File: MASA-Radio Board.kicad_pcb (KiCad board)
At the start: 4 copper layers, 75.8 x 76.2 mm, 71 parts, among them IC1 FAN4010IL6X_F113, IC2 FAN4010IL6X_F113, J1 Conn_01x02, J2 Conn_01x02_Male, J3 Conn_01x02_Male, J4 Conn_01x03_Male, J5 Conn_01x06, J6 SC_19-20, J7 Conn_01x06, J8 Conn_01x02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

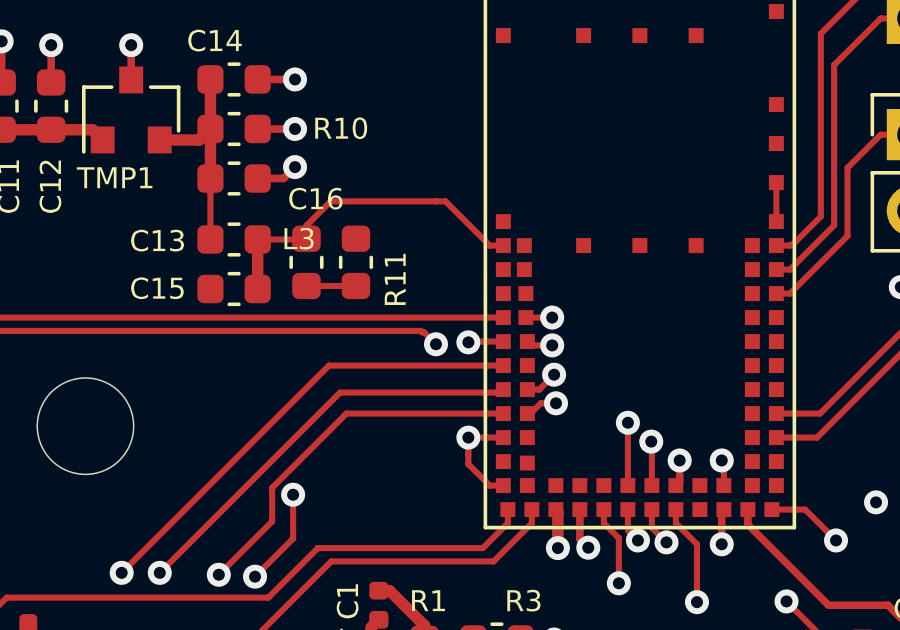
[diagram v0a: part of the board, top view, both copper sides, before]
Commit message: fixed tsense
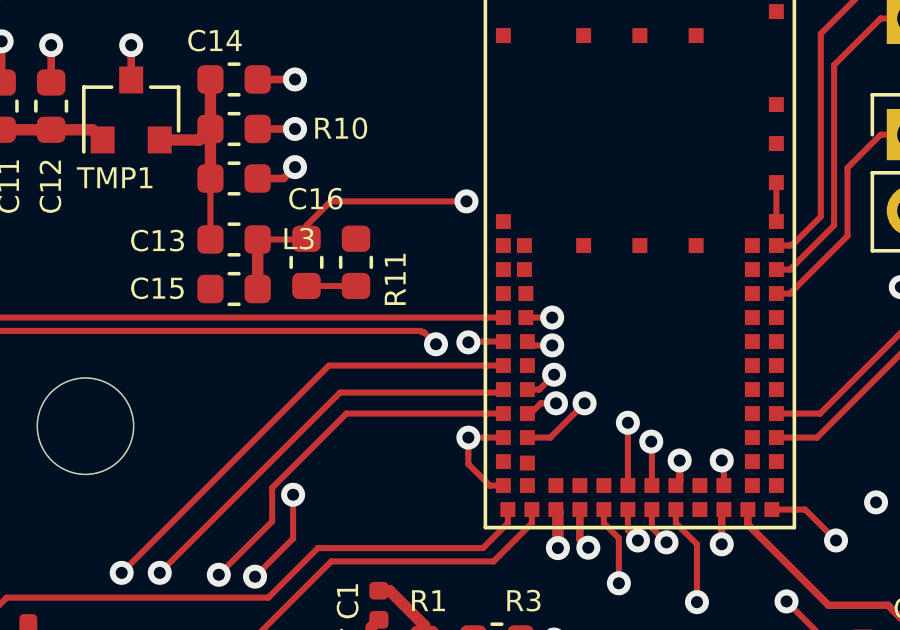
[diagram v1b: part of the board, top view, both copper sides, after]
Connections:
- U2 pad 48: Net-(U2-Pad48) -> TSENSE
- U2 pad 63: TSENSE -> Net-(U2-Pad63)
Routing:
- net TSENSE: track 11.2 -> 20.1 mm, vias 0 -> 2
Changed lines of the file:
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@@
     (thickness 1.6)
     (drawings 18)
-    (tracks 702)
+    (tracks 707)
     (zones 0)
     (modules 71)
@@
   (net 38 "Net-(U2-Pad60)")
   (net 39 "Net-(U2-Pad54)")
-  (net 40 "Net-(U2-Pad48)")
-  (net 41 "Net-(U2-Pad46)")
+  (net 40 "Net-(U2-Pad46)")
+  (net 41 "Net-(U2-Pad63)")
   (net 42 "Net-(U2-Pad61)")
   (net 43 "Net-(U2-Pad59)")
@@
     (add_net "Net-(U2-Pad45)")
     (add_net "Net-(U2-Pad46)")
-    (add_net "Net-(U2-Pad48)")
     (add_net "Net-(U2-Pad54)")
     (add_net "Net-(U2-Pad59)")
@@
     (add_net "Net-(U2-Pad61)")
     (add_net "Net-(U2-Pad62)")
+    (add_net "Net-(U2-Pad63)")
     (add_net "Net-(U2-Pad64)")
     (add_net "Net-(U2-Pad7)")
@@
       (net 26 TX2RTS))
     (pad 48 smd rect (at -3.75 8.15) (size 0.5 0.5) (layers F.Cu F.Paste F.Mask)
-      (net 40 "Net-(U2-Pad48)"))
+      (net 72 TSENSE))
     (pad 46 smd rect (at -3.75 9) (size 0.5 0.5) (layers F.Cu F.Paste F.Mask)
-      (net 41 "Net-(U2-Pad46)"))
+      (net 40 "Net-(U2-Pad46)"))
     (pad 65 smd rect (at -4.55 0.95) (size 0.5 0.5) (layers F.Cu F.Paste F.Mask)
       (net 1 GND))
     (pad 63 smd rect (at -4.55 1.75) (size 0.5 0.5) (layers F.Cu F.Paste F.Mask)
-      (net 72 TSENSE))
+      (net 41 "Net-(U2-Pad63)"))
     (pad 61 smd rect (at -4.55 2.55) (size 0.5 0.5) (layers F.Cu F.Paste F.Mask)
       (net 42 "Net-(U2-Pad61)"))
@@
   (segment (start 152.7 109.107114) (end 152.700889 109.106225) (width 0.2032) (layer F.Cu) (net 14))
   (segment (start 152.7 111.2) (end 152.7 109.107114) (width 0.2032) (layer F.Cu) (net 14))
-  (segment (start 152.700889 109.106225) (end 150.418275 109.106225) (width 0.2032) (layer In2.Cu) (net 14))
-  (segment (start 147.193 112.3315) (end 128.9685 112.3315) (width 0.2032) (layer In2.Cu) (net 14))
-  (segment (start 150.418275 109.106225) (end 147.193 112.3315) (width 0.2032) (layer In2.Cu) (net 14))
-  (segment (start 128.9685 112.3315) (end 126.746 114.554) (width 0.2032) (layer In2.Cu) (net 14))
+  (segment (start 150.418275 109.106225) (end 152.700889 109.106225) (width 0.2032) (layer In2.Cu) (net 14))
+  (segment (start 126.746 114.554) (end 128.7145 112.5855) (width 0.2032) (layer In2.Cu) (net 14))
+  (segment (start 146.939 112.5855) (end 150.418275 109.106225) (width 0.2032) (layer In2.Cu) (net 14))
+  (segment (start 128.7145 112.5855) (end 146.939 112.5855) (width 0.2032) (layer In2.Cu) (net 14))
   (segment (start 153.5 111.2) (end 153.5 111.168) (width 0.254) (layer F.Cu) (net 15))
   (via (at 127.889 114.681) (size 0.8) (drill 0.4) (layers F.Cu B.Cu) (net 15))
@@
   (segment (start 153.5 111.2) (end 153.5 109.755325) (width 0.2032) (layer F.Cu) (net 15))
   (segment (start 153.5 109.755325) (end 153.4795 109.734825) (width 0.2032) (layer F.Cu) (net 15))
-  (segment (start 153.4795 109.734825) (end 150.424675 109.734825) (width 0.2032) (layer In2.Cu) (net 15))
-  (segment (start 150.424675 109.734825) (end 147.3835 112.776) (width 0.2032) (layer In2.Cu) (net 15))
-  (segment (start 147.3835 112.776) (end 129.794 112.776) (width 0.2032) (layer In2.Cu) (net 15))
-  (segment (start 129.794 112.776) (end 127.889 114.681) (width 0.2032) (layer In2.Cu) (net 15))
+  (segment (start 150.424675 109.734825) (end 153.4795 109.734825) (width 0.2032) (layer In2.Cu) (net 15))
+  (segment (start 147.1295 113.03) (end 150.424675 109.734825) (width 0.2032) (layer In2.Cu) (net 15))
+  (segment (start 127.889 114.681) (end 129.54 113.03) (width 0.2032) (layer In2.Cu) (net 15))
+  (segment (start 129.54 113.03) (end 147.1295 113.03) (width 0.2032) (layer In2.Cu) (net 15))
   (segment (start 154.3 111.2) (end 154.253 111.2) (width 0.254) (layer F.Cu) (net 16))
   (via (at 154.426471 110.363425) (size 0.8) (drill 0.4) (layers F.Cu B.Cu) (net 16))
@@
   (via (at 129.032 114.681) (size 0.8) (drill 0.4) (layers F.Cu B.Cu) (net 16))
   (segment (start 128.905 114.808) (end 129.032 114.681) (width 0.254) (layer F.Cu) (net 16))
-  (segment (start 130.3655 113.3475) (end 147.701 113.3475) (width 0.2032) (layer In2.Cu) (net 16))
-  (segment (start 150.685075 110.363425) (end 154.426471 110.363425) (width 0.2032) (layer In2.Cu) (net 16))
-  (segment (start 147.701 113.3475) (end 150.685075 110.363425) (width 0.2032) (layer In2.Cu) (net 16))
-  (segment (start 129.032 114.681) (end 130.3655 113.3475) (width 0.2032) (layer In2.Cu) (net 16))
+  (segment (start 129.032 114.681) (end 130.232101 113.480899) (width 0.2032) (layer In2.Cu) (net 16))
+  (segment (start 150.685075 110.363425) (end 147.574 113.4745) (width 0.2032) (layer In2.Cu) (net 16))
+  (segment (start 130.232101 113.480899) (end 147.32 113.4745) (width 0.2032) (layer In2.Cu) (net 16))
+  (segment (start 147.574 113.4745) (end 147.32 113.4745) (width 0.2032) (layer In2.Cu) (net 16))
+  (segment (start 154.426471 110.363425) (end 150.685075 110.363425) (width 0.2032) (layer In2.Cu) (net 16))
+  (segment (start 147.32 113.4745) (end 147.504101 113.480899) (width 0.2032) (layer In2.Cu) (net 16))
   (via (at 155.0035 115.085801) (size 0.8) (drill 0.4) (layers F.Cu B.Cu) (net 17))
   (segment (start 155.0035 114.520116) (end 155.0035 115.085801) (width 0.2032) (layer F.Cu) (net 17))
@@
   (segment (start 141.9605 102.997) (end 141.986 102.9715) (width 0.2032) (layer F.Cu) (net 72))
   (segment (start 140.3605 102.997) (end 141.9605 102.997) (width 0.2032) (layer F.Cu) (net 72))
-  (segment (start 141.986 102.534) (end 142.793 101.727) (width 0.2032) (layer F.Cu) (net 72))
-  (segment (start 141.986 102.9715) (end 141.986 102.534) (width 0.2032) (layer F.Cu) (net 72))
-  (segment (start 146.6238 101.727) (end 146.304 101.727) (width 0.2032) (layer F.Cu) (net 72))
-  (segment (start 148.0968 103.2) (end 146.6238 101.727) (width 0.2032) (layer F.Cu) (net 72))
-  (segment (start 148.55 103.2) (end 148.0968 103.2) (width 0.2032) (layer F.Cu) (net 72))
-  (segment (start 142.793 101.727) (end 146.304 101.727) (width 0.2032) (layer F.Cu) (net 72))
+  (via (at 147.32 101.727) (size 0.8) (drill 0.4) (layers F.Cu B.Cu) (net 72))
+  (segment (start 141.986 102.534) (end 141.986 102.9715) (width 0.2032) (layer F.Cu) (net 72))
+  (segment (start 147.32 101.727) (end 142.793 101.727) (width 0.2032) (layer F.Cu) (net 72))
+  (segment (start 142.793 101.727) (end 141.986 102.534) (width 0.2032) (layer F.Cu) (net 72))
+  (via (at 151.257 108.458) (size 0.8) (drill 0.4) (layers F.Cu B.Cu) (net 72))
+  (segment (start 151.257 108.458) (end 150.115 109.6) (width 0.2032) (layer F.Cu) (net 72))
+  (segment (start 150.115 109.6) (end 149.35 109.6) (width 0.2032) (layer F.Cu) (net 72))
+  (segment (start 151.257 105.664) (end 147.32 101.727) (width 0.2032) (layer In2.Cu) (net 72))
+  (segment (start 151.257 108.458) (end 151.257 105.664) (width 0.2032) (layer In2.Cu) (net 72))
   (segment (start 174.609 130.0385) (end 175.768 128.8795) (width 0.2032) (layer F.Cu) (net 74))
   (segment (start 174.609 130.206) (end 174.609 130.0385) (width 0.2032) (layer F.Cu) (net 74))

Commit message: Added caps on 3.3V MCU
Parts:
- added C26: 100uF, Capacitor_SMD:C_0603_1608Metric, F.Cu at (165.0, 116.2)
- added C27: 1uF, Capacitor_SMD:C_0603_1608Metric, F.Cu at (169.0, 116.2)
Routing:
- net +3V3: track 25.6 -> 42.9 mm, vias 5 -> 6
- net GND: track 106.6 -> 109.2 mm, vias 59 -> 61
- net V_IN_5V0: track 113.1 -> 112.2 mm
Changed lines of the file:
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@@
     (thickness 1.6)
     (drawings 18)
-    (tracks 707)
+    (tracks 718)
     (zones 0)
-    (modules 71)
+    (modules 73)
     (nets 134)
   )
@@
     (add_net nAutoRun)
   )
+  (module Capacitor_SMD:C_0603_1608Metric (layer F.Cu)
+    (at 169.0465 116.205)
+    (descr "Capacitor SMD 0603 (1608 Metric), square (rectangular) end terminal, IPC_7351 nominal, (Body size source: http://www.tortai-tech.com/upload/download/2011102023233369053.pdf), generated with kicad-footprint-generator")
+    (tags capacitor)
+    (attr smd)
+    (fp_text reference C27 (at 0.7525 -1.4605) (layer F.SilkS)
+      (effects (font (size 1 1) (thickness 0.15)))
+    )
+    (fp_text value 1uF (at 0 1.43) (layer F.Fab)
+      (effects (font (size 1 1) (thickness 0.15)))
+    )
+    (fp_line (start -0.8 0.4) (end -0.8 -0.4) (layer F.Fab) (width 0.1))
+    (fp_line (start -0.8 -0.4) (end 0.8 -0.4) (layer F.Fab) (width 0.1))
+    (fp_line (start 0.8 -0.4) (end 0.8 0.4) (layer F.Fab) (width 0.1))
+    (fp_line (start 0.8 0.4) (end -0.8 0.4) (layer F.Fab) (width 0.1))
+    (fp_line (start -0.162779 -0.51) (end 0.162779 -0.51) (layer F.SilkS) (width 0.12))
+    (fp_line (start -0.162779 0.51) (end 0.162779 0.51) (layer F.SilkS) (width 0.12))
+    (fp_line (start -1.48 0.73) (end -1.48 -0.73) (layer F.CrtYd) (width 0.05))
+    (fp_line (start -1.48 -0.73) (end 1.48 -0.73) (layer F.CrtYd) (width 0.05))
+    (fp_line (start 1.48 -0.73) (end 1.48 0.73) (layer F.CrtYd) (width 0.05))
+    (fp_line (start 1.48 0.73) (end -1.48 0.73) (layer F.CrtYd) (width 0.05))
+    (fp_text user %R (at 0 0) (layer F.Fab)
+      (effects (font (size 0.4 0.4) (thickness 0.06)))
+    )
+    (pad 1 smd roundrect (at -0.7875 0) (size 0.875 0.95) (layers F.Cu F.Paste F.Mask) (roundrect_rratio 0.25)
+      (net 8 +3V3))
+    (pad 2 smd roundrect (at 0.7875 0) (size 0.875 0.95) (layers F.Cu F.Paste F.Mask) (roundrect_rratio 0.25)
+      (net 1 GND))
+    (model ${KISYS3DMOD}/Capacitor_SMD.3dshapes/C_0603_1608Metric.wrl
+      (at (xyz 0 0 0))
+      (scale (xyz 1 1 1))
+      (rotate (xyz 0 0 0))
+    )
+  )
+  (module Capacitor_SMD:C_0603_1608Metric (layer F.Cu)
+    (at 165.0365 116.205)
+    (descr "Capacitor SMD 0603 (1608 Metric), square (rectangular) end terminal, IPC_7351 nominal, (Body size source: http://www.tortai-tech.com/upload/download/2011102023233369053.pdf), generated with kicad-footprint-generator")
+    (tags capacitor)
+    (attr smd)
+    (fp_text reference C26 (at 0.889 -1.4605) (layer F.SilkS)
+      (effects (font (size 1 1) (thickness 0.15)))
+    )
+    (fp_text value 100uF (at 0 1.43) (layer F.Fab)
+      (effects (font (size 1 1) (thickness 0.15)))
+    )
+    (fp_line (start -0.8 0.4) (end -0.8 -0.4) (layer F.Fab) (width 0.1))
+    (fp_line (start -0.8 -0.4) (end 0.8 -0.4) (layer F.Fab) (width 0.1))
+    (fp_line (start 0.8 -0.4) (end 0.8 0.4) (layer F.Fab) (width 0.1))
+    (fp_line (start 0.8 0.4) (end -0.8 0.4) (layer F.Fab) (width 0.1))
+    (fp_line (start -0.162779 -0.51) (end 0.162779 -0.51) (layer F.SilkS) (width 0.12))
+    (fp_line (start -0.162779 0.51) (end 0.162779 0.51) (layer F.SilkS) (width 0.12))
+    (fp_line (start -1.48 0.73) (end -1.48 -0.73) (layer F.CrtYd) (width 0.05))
+    (fp_line (start -1.48 -0.73) (end 1.48 -0.73) (layer F.CrtYd) (width 0.05))
+    (fp_line (start 1.48 -0.73) (end 1.48 0.73) (layer F.CrtYd) (width 0.05))
+    (fp_line (start 1.48 0.73) (end -1.48 0.73) (layer F.CrtYd) (width 0.05))
+    (fp_text user %R (at 0 0) (layer F.Fab)
+      (effects (font (size 0.4 0.4) (thickness 0.06)))
+    )
+    (pad 1 smd roundrect (at -0.7875 0) (size 0.875 0.95) (layers F.Cu F.Paste F.Mask) (roundrect_rratio 0.25)
+      (net 8 +3V3))
+    (pad 2 smd roundrect (at 0.7875 0) (size 0.875 0.95) (layers F.Cu F.Paste F.Mask) (roundrect_rratio 0.25)
+      (net 1 GND))
+    (model ${KISYS3DMOD}/Capacitor_SMD.3dshapes/C_0603_1608Metric.wrl
+      (at (xyz 0 0 0))
+      (scale (xyz 1 1 1))
+      (rotate (xyz 0 0 0))
+    )
+  )
   (module Connector_PinHeader_2.54mm:PinHeader_1x06_P2.54mm_Vertical (layer F.Cu)
     (at 179.959 104.267 230)
@@
   (segment (start 149.35 108) (end 149.7465 108) (width 0.2032) (layer F.Cu) (net 1))
   (segment (start 149.7465 108) (end 150.241 107.5055) (width 0.2032) (layer F.Cu) (net 1))
+  (via (at 167.0685 116.205) (size 0.8) (drill 0.4) (layers F.Cu B.Cu) (net 1))
+  (segment (start 165.824 116.205) (end 167.0685 116.205) (width 0.2032) (layer F.Cu) (net 1))
+  (via (at 171.196 116.205) (size 0.8) (drill 0.4) (layers F.Cu B.Cu) (net 1))
+  (segment (start 169.834 116.205) (end 171.196 116.205) (width 0.2032) (layer F.Cu) (net 1))
   (segment (start 160.655 126.4742) (end 161.925 127.7442) (width 0.2032) (layer F.Cu) (net 2))
   (segment (start 160.655 126.3142) (end 160.655 126.4742) (width 0.2032) (layer F.Cu) (net 2))
@@
   (segment (start 130.683 128.524) (end 132.461 128.524) (width 0.381) (layer F.Cu) (net 8))
   (segment (start 129.747 129.46) (end 130.1115 129.0955) (width 0.381) (layer F.Cu) (net 8))
-  (segment (start 155.9 112) (end 155.9 112.085) (width 0.25) (layer F.Cu) (net 8))
-  (via (at 155.829 113.157) (size 0.8) (drill 0.4) (layers F.Cu B.Cu) (net 8))
-  (segment (start 155.9 112.085) (end 155.829 112.156) (width 0.25) (layer F.Cu) (net 8))
-  (segment (start 155.829 112.156) (end 155.829 113.157) (width 0.25) (layer F.Cu) (net 8))
   (via (at 150.241 116.332) (size 0.8) (drill 0.4) (layers F.Cu B.Cu) (net 8))
   (segment (start 149.1235 116.332) (end 150.241 116.332) (width 0.2032) (layer F.Cu) (net 8))
@@
   (via (at 161.798 104.5845) (size 0.8) (drill 0.4) (layers F.Cu B.Cu) (net 8))
   (segment (start 162.179 104.2035) (end 161.798 104.5845) (width 0.2032) (layer F.Cu) (net 8))
+  (via (at 158.623 116.459) (size 0.8) (drill 0.4) (layers F.Cu B.Cu) (net 8))
+  (segment (start 155.9 112) (end 155.9 113.736) (width 0.2032) (layer F.Cu) (net 8))
+  (segment (start 155.9 113.736) (end 158.623 116.459) (width 0.2032) (layer F.Cu) (net 8))
+  (via (at 163.83 114.7445) (size 0.8) (drill 0.4) (layers F.Cu B.Cu) (net 8))
+  (segment (start 158.623 116.459) (end 160.3375 114.7445) (width 0.2032) (layer In2.Cu) (net 8))
+  (segment (start 160.3375 114.7445) (end 163.83 114.7445) (width 0.2032) (layer In2.Cu) (net 8))
+  (segment (start 163.83 115.786) (end 164.249 116.205) (width 0.2032) (layer F.Cu) (net 8))
+  (segment (start 163.83 114.7445) (end 163.83 115.786) (width 0.2032) (layer F.Cu) (net 8))
+  (segment (start 168.259 115.73) (end 168.259 116.205) (width 0.2032) (layer F.Cu) (net 8))
+  (segment (start 167.2735 114.7445) (end 168.259 115.73) (width 0.2032) (layer F.Cu) (net 8))
+  (segment (start 163.83 114.7445) (end 167.2735 114.7445) (width 0.2032) (layer F.Cu) (net 8))
   (segment (start 148.352 118.5092) (end 148.4608 118.618) (width 0.2032) (layer F.Cu) (net 10))
   (segment (start 148.352 118.206) (end 148.352 118.5092) (width 0.2032) (layer F.Cu) (net 10))
@@
   (segment (start 159.197 119.314) (end 161.13833 119.314) (width 0.2032) (layer In2.Cu) (net 71))
   (segment (start 163.351931 117.100399) (end 170.313399 117.100399) (width 0.2032) (layer In2.Cu) (net 71))
-  (via (at 157.988 115.062) (size 0.8) (drill 0.4) (layers F.Cu B.Cu) (net 71))
-  (segment (start 159.451 116.525) (end 157.988 115.062) (width 0.2032) (layer F.Cu) (net 71))
+  (via (at 158.4325 115.1255) (size 0.8) (drill 0.4) (layers F.Cu B.Cu) (net 71))
   (segment (start 159.451 117.414) (end 159.451 116.525) (width 0.2032) (layer F.Cu) (net 71))
   (segment (start 174.865413 101.001639) (end 176.067494 101.001639) (width 0.2032) (layer In2.Cu) (net 71))
   (segment (start 172.614046 101.001639) (end 174.865413 101.001639) (width 0.2032) (layer In2.Cu) (net 71))
   (segment (start 158.553685 115.062) (end 172.614046 101.001639) (width 0.2032) (layer In2.Cu) (net 71))
-  (segment (start 157.988 115.062) (end 158.553685 115.062) (width 0.2032) (layer In2.Cu) (net 71))
+  (segment (start 159.451 116.144) (end 159.451 116.525) (width 0.2032) (layer F.Cu) (net 71))
+  (segment (start 158.4325 115.1255) (end 159.451 116.144) (width 0.2032) (layer F.Cu) (net 71))
   (segment (start 140.3605 102.997) (end 140.3605 104.648) (width 0.381) (layer F.Cu) (net 72))
   (segment (start 141.9605 102.997) (end 141.986 102.9715) (width 0.2032) (layer F.Cu) (net 72))

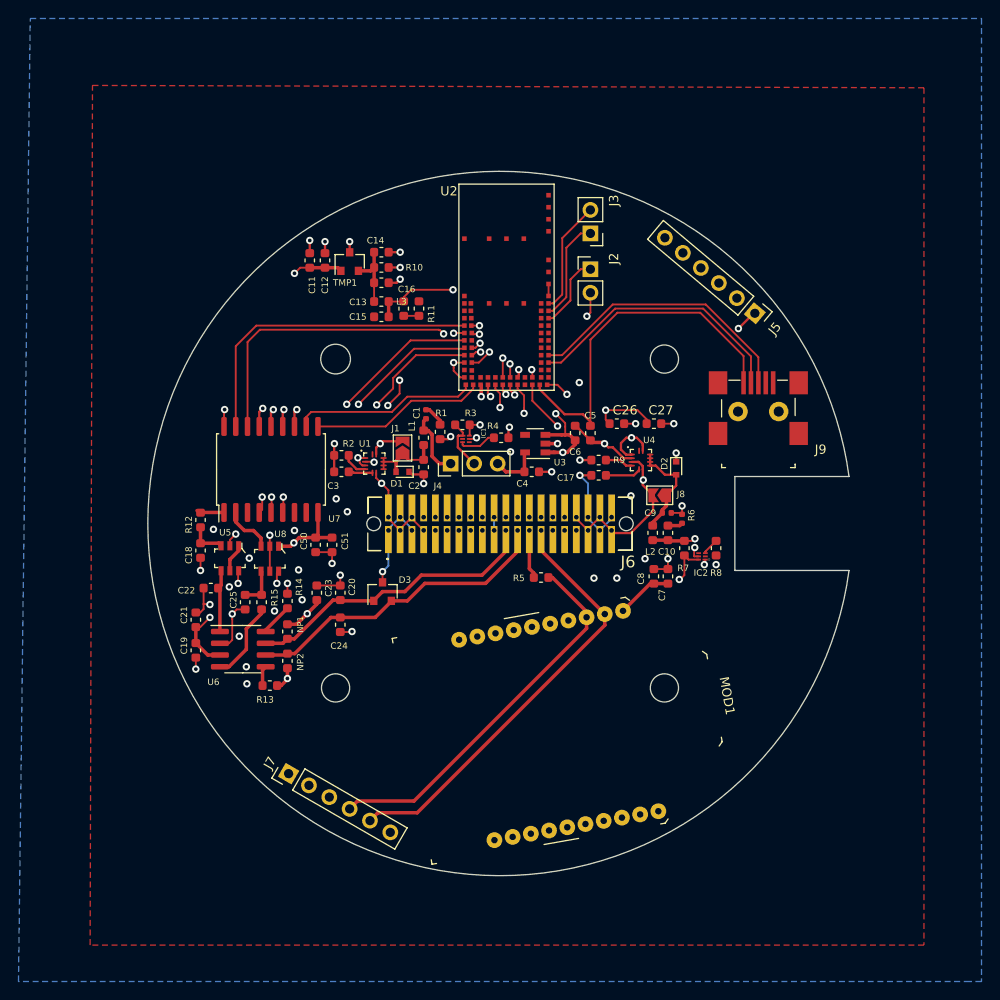
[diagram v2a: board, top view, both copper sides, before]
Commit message: Fixed caps and added grounding
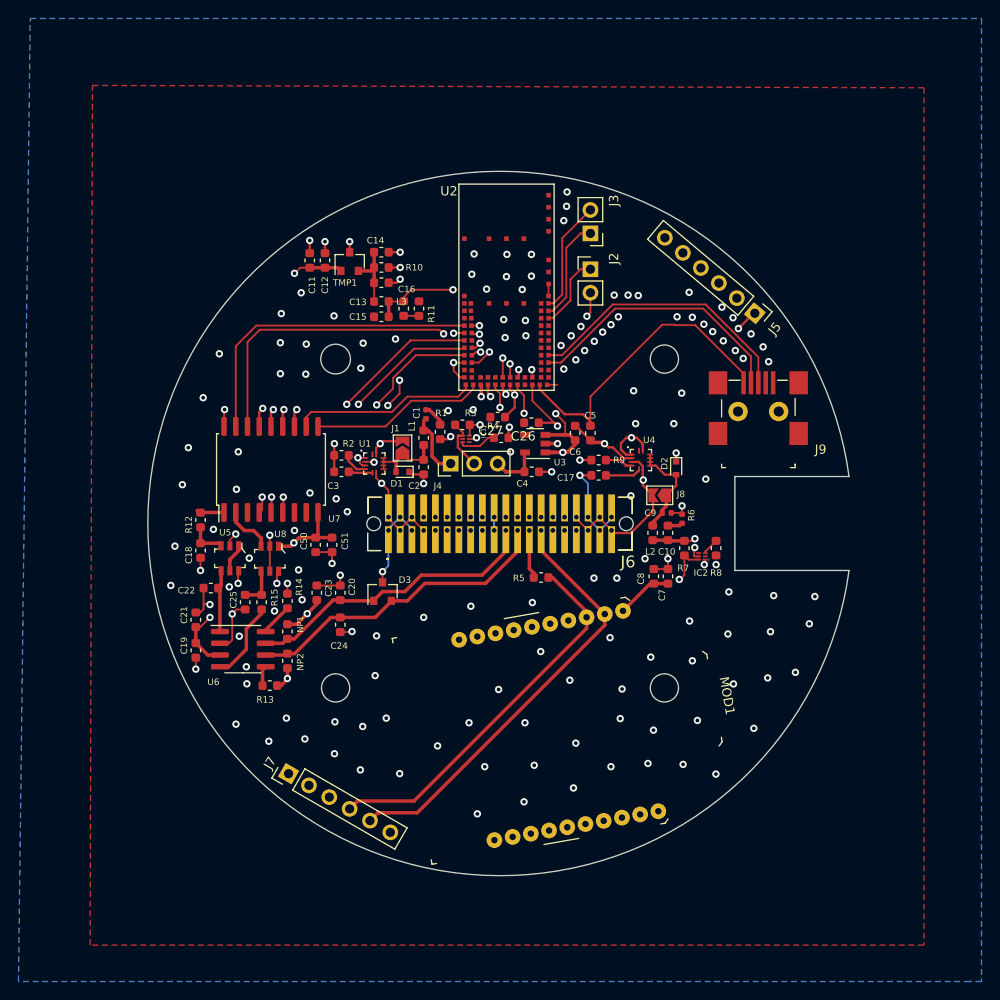
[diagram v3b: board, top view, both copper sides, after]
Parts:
- C26: value 100uF -> 100nF
- C27: value 1uF -> 1nF
- moved C27 16.9 mm to (152.2, 115.5), turned to 180 degrees
- moved C26 9.24 mm to (155.8, 116.1), turned to 180 degrees
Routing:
- net +3V3: track 42.9 -> 35.0 mm, vias 6 -> 5
- net USB_VBUS: track 39.8 -> 34.0 mm
- net GND: track 109.2 -> 105.2 mm, vias 61 -> 173
- net MCU_TX: track 30.1 -> 31.8 mm
- added copper zone on In2.Cu, net GND
